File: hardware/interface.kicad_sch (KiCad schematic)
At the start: 26 parts, among them P1 TS2068_Edge, SW1 TS Reset, SW2 NMI, U1 74LVC245APW, U12 74LVC574APW, U13 74LVC574APW, U2 74LVC245APW, U3 74LVC245APW, U4 74LVC245APW, U6 74LVC32APW, U7 74LVC06AD, U8 74LVC245APW, U9 74LVC1G86

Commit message: Drop the DMA option: board fully routed, zero DRC errors
DMA_OPTION = False removes U8, U9, U12, U13 and six GPIOs; the data transceiver
takes DIR from /RD with its A side on the Z80 bus. Rerouted with the scripted
flow; finish order is DVDD before +3V3, supply pin 29 escapes through the freed
pad lanes, DVDD widened to 0.25 mm. No signal on either plane layer, all vias
0.6/0.3. Fab outputs regenerated; parts + fees $14.48 per board at 10 boards.

Co-Authored-By: Claude Fable 5.1 <noreply@anthropic.com>
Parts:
- removed C7, C8, C9: 100n, Capacitor_SMD:C_0603_1608Metric, symbol Device:C
- removed R4: 10k, Resistor_SMD:R_0603_1608Metric, symbol Device:R
- removed U12, U13: 74LVC574APW, Package_SO:TSSOP-20_4.4x6.5mm_P0.65mm, symbol 74xx:74LS574
- removed U8: 74LVC245APW, Package_SO:TSSOP-20_4.4x6.5mm_P0.65mm, symbol 74xx:74LS245
- removed U9: 74LVC1G86, Package_TO_SOT_SMD:SOT-23-5, symbol 74xGxx:74LVC1G86
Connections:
- net DATA_DIR is gone; now on net nRD: U3.1 (A->B)
- net D0: now also U3.3 (A1); no longer U3.12 (B6)
- net D1: now also U3.4 (A2); no longer U3.13 (B5)
- net D2: now also U3.5 (A3); no longer U3.14 (B4)
- net D3: now also U3.8 (A6); no longer U3.17 (B1)
- net D4: now also U3.9 (A7); no longer U3.18 (B0)
- net D5: now also U3.7 (A5); no longer U3.16 (B2)
- net D6: now also U3.6 (A4); no longer U3.15 (B3)
- net D7: now also U3.2 (A0); no longer U3.11 (B7)
- net MD0: now also U3.17 (B1); no longer U3.8 (A6)
- net MD1: now also U3.16 (B2); no longer U3.7 (A5)
- net MD2: now also U3.15 (B3); no longer U3.6 (A4)
- net MD3: now also U3.12 (B6); no longer U3.3 (A1)
- net MD4: now also U3.11 (B7); no longer U3.2 (A0)
- net MD5: now also U3.13 (B5); no longer U3.4 (A2)
- net MD6: now also U3.14 (B4); no longer U3.5 (A3)
- net MD7: now also U3.18 (B0); no longer U3.9 (A7)
- no-connect marks 21 -> 16

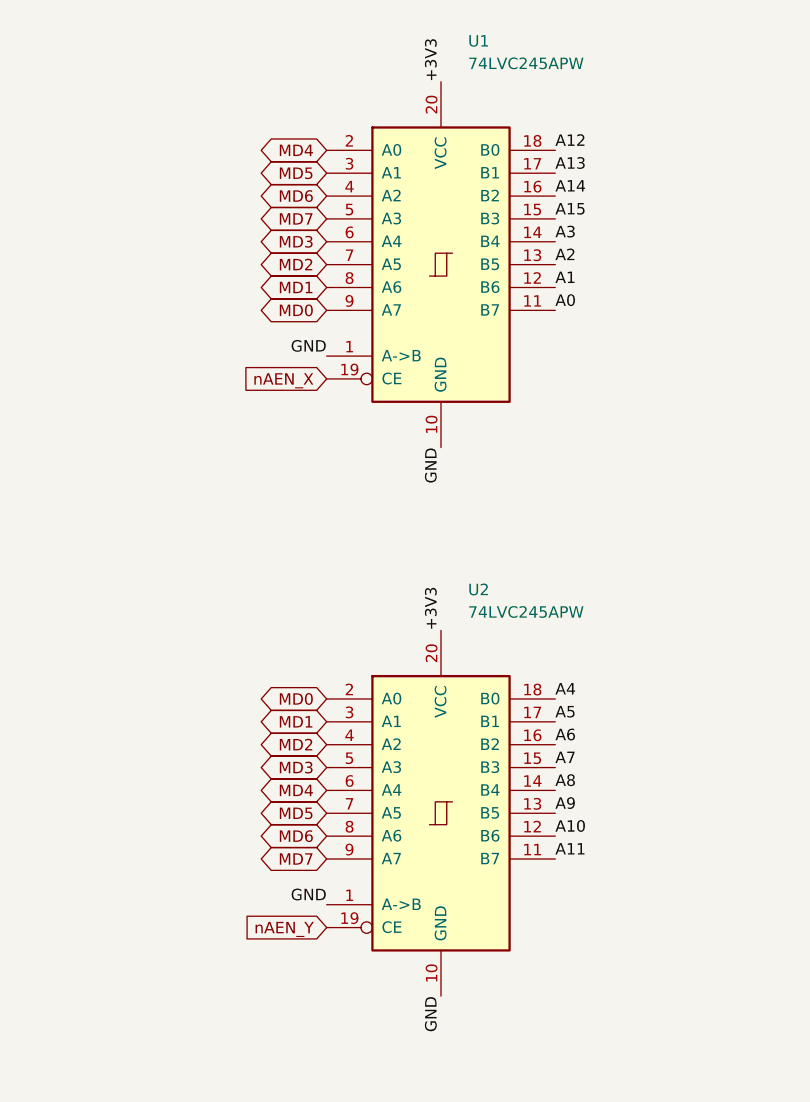
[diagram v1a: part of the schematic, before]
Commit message: Plain address bytes in hardware; DVDD spine and bottom-row fan pre-routed
U1 delivers A0-A7 and U2 A8-A15 on MD0-MD7 (U2 over its fingers, U1 in the row
above fed from both sides), so the firmware sees ordinary addresses. preroute.py
now also fixes the DVDD spine under the package, the inner 3.3 V supply links,
pin 51's capacitor and a deterministic fan for the fully used bottom pad row.
OLED_DC moves to GP34. Exposed pad gets five ground vias. finish.py: DVDD first,
clearance-aware widening, hairline fixes, unused-via cleanup, overlapping pads.
Fully routed, zero DRC errors; fab outputs regenerated.

Co-Authored-By: Claude Fable 5.1 <noreply@anthropic.com>
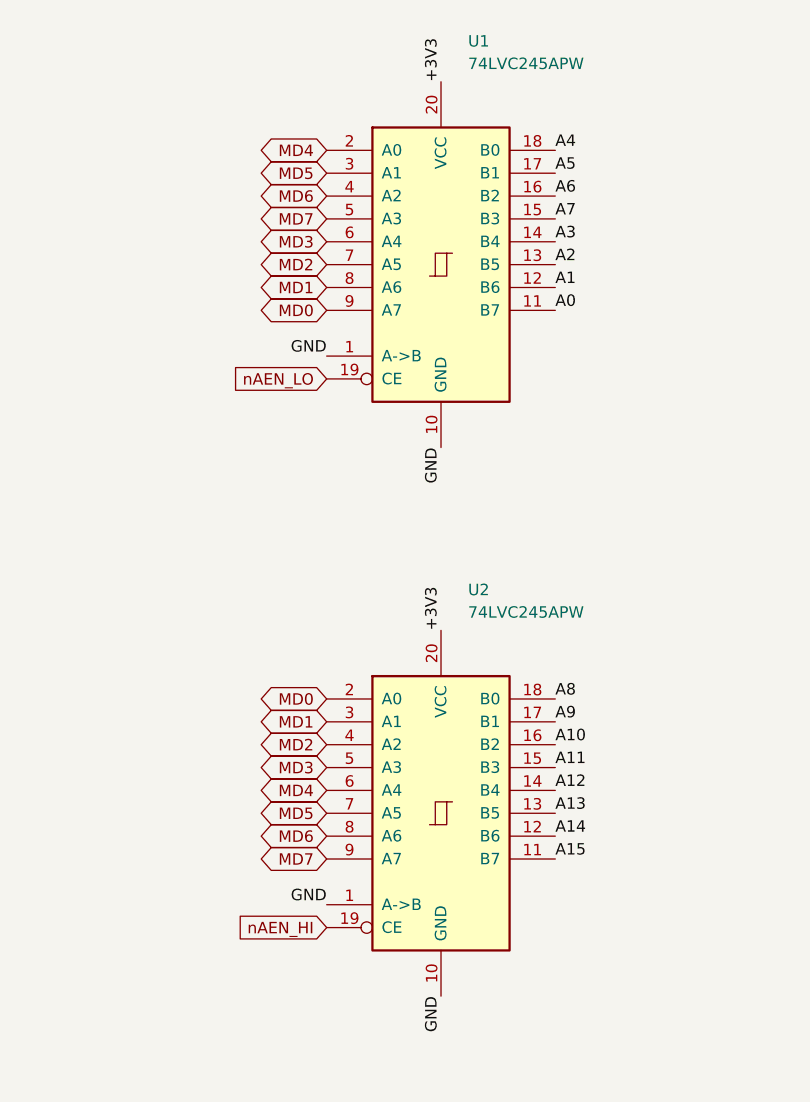
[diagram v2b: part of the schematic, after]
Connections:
- net A10: now also U2.16 (B2); no longer U2.12 (B6)
- net A11: now also U2.15 (B3); no longer U2.11 (B7)
- net A12: now also U2.14 (B4); no longer U1.18 (B0)
- net A13: now also U2.13 (B5); no longer U1.17 (B1)
- net A14: now also U2.12 (B6); no longer U1.16 (B2)
- net A15: now also U2.11 (B7); no longer U1.15 (B3)
- net A4: now also U1.18 (B0); no longer U2.18 (B0)
- net A5: now also U1.17 (B1); no longer U2.17 (B1)
- net A6: now also U1.16 (B2); no longer U2.16 (B2)
- net A7: now also U1.15 (B3); no longer U2.15 (B3)
- net A8: now also U2.18 (B0); no longer U2.14 (B4)
- net A9: now also U2.17 (B1); no longer U2.13 (B5)
- net nAEN_X renamed nAEN_LO
- net nAEN_Y renamed nAEN_HI
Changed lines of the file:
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@@
   (label "A3" (at 162.56 46.99 0) (effects (font (size 1.27 1.27)) (justify left bottom)))
   (global_label "MD3" (shape bidirectional) (at 137.16 46.99 180) (effects (font (size 1.27 1.27)) (justify right)))
-  (label "A15" (at 162.56 44.45 0) (effects (font (size 1.27 1.27)) (justify left bottom)))
+  (label "A7" (at 162.56 44.45 0) (effects (font (size 1.27 1.27)) (justify left bottom)))
   (global_label "MD7" (shape bidirectional) (at 137.16 44.45 180) (effects (font (size 1.27 1.27)) (justify right)))
-  (label "A14" (at 162.56 41.91 0) (effects (font (size 1.27 1.27)) (justify left bottom)))
+  (label "A6" (at 162.56 41.91 0) (effects (font (size 1.27 1.27)) (justify left bottom)))
   (global_label "MD6" (shape bidirectional) (at 137.16 41.91 180) (effects (font (size 1.27 1.27)) (justify right)))
-  (label "A13" (at 162.56 39.37 0) (effects (font (size 1.27 1.27)) (justify left bottom)))
+  (label "A5" (at 162.56 39.37 0) (effects (font (size 1.27 1.27)) (justify left bottom)))
   (global_label "MD5" (shape bidirectional) (at 137.16 39.37 180) (effects (font (size 1.27 1.27)) (justify right)))
-  (label "A12" (at 162.56 36.83 0) (effects (font (size 1.27 1.27)) (justify left bottom)))
+  (label "A4" (at 162.56 36.83 0) (effects (font (size 1.27 1.27)) (justify left bottom)))
   (global_label "MD4" (shape bidirectional) (at 137.16 36.83 180) (effects (font (size 1.27 1.27)) (justify right)))
   (label "GND" (at 137.16 59.69 180) (effects (font (size 1.27 1.27)) (justify right bottom)))
-  (global_label "nAEN_X" (shape input) (at 137.16 62.23 180) (effects (font (size 1.27 1.27)) (justify right)))
+  (global_label "nAEN_LO" (shape input) (at 137.16 62.23 180) (effects (font (size 1.27 1.27)) (justify right)))
   (label "+3V3" (at 149.86 29.21 90) (effects (font (size 1.27 1.27)) (justify left bottom)))
   (label "GND" (at 149.86 69.85 270) (effects (font (size 1.27 1.27)) (justify right bottom)))
@@
     (instances (project "tspico-v3" (path "/9088d141-8624-4d5c-91a9-7a3a7a90b3cc/a611a6fb-5e55-4c31-9c90-ae90d05d13a4" (reference "U2") (unit 1))))
   )
-  (label "A11" (at 162.56 115.57 0) (effects (font (size 1.27 1.27)) (justify left bottom)))
+  (label "A15" (at 162.56 115.57 0) (effects (font (size 1.27 1.27)) (justify left bottom)))
   (global_label "MD7" (shape bidirectional) (at 137.16 115.57 180) (effects (font (size 1.27 1.27)) (justify right)))
-  (label "A10" (at 162.56 113.03 0) (effects (font (size 1.27 1.27)) (justify left bottom)))
+  (label "A14" (at 162.56 113.03 0) (effects (font (size 1.27 1.27)) (justify left bottom)))
   (global_label "MD6" (shape bidirectional) (at 137.16 113.03 180) (effects (font (size 1.27 1.27)) (justify right)))
-  (label "A9" (at 162.56 110.49 0) (effects (font (size 1.27 1.27)) (justify left bottom)))
+  (label "A13" (at 162.56 110.49 0) (effects (font (size 1.27 1.27)) (justify left bottom)))
   (global_label "MD5" (shape bidirectional) (at 137.16 110.49 180) (effects (font (size 1.27 1.27)) (justify right)))
-  (label "A8" (at 162.56 107.95 0) (effects (font (size 1.27 1.27)) (justify left bottom)))
+  (label "A12" (at 162.56 107.95 0) (effects (font (size 1.27 1.27)) (justify left bottom)))
   (global_label "MD4" (shape bidirectional) (at 137.16 107.95 180) (effects (font (size 1.27 1.27)) (justify right)))
-  (label "A7" (at 162.56 105.41 0) (effects (font (size 1.27 1.27)) (justify left bottom)))
+  (label "A11" (at 162.56 105.41 0) (effects (font (size 1.27 1.27)) (justify left bottom)))
   (global_label "MD3" (shape bidirectional) (at 137.16 105.41 180) (effects (font (size 1.27 1.27)) (justify right)))
-  (label "A6" (at 162.56 102.87 0) (effects (font (size 1.27 1.27)) (justify left bottom)))
+  (label "A10" (at 162.56 102.87 0) (effects (font (size 1.27 1.27)) (justify left bottom)))
   (global_label "MD2" (shape bidirectional) (at 137.16 102.87 180) (effects (font (size 1.27 1.27)) (justify right)))
-  (label "A5" (at 162.56 100.33 0) (effects (font (size 1.27 1.27)) (justify left bottom)))
+  (label "A9" (at 162.56 100.33 0) (effects (font (size 1.27 1.27)) (justify left bottom)))
   (global_label "MD1" (shape bidirectional) (at 137.16 100.33 180) (effects (font (size 1.27 1.27)) (justify right)))
-  (label "A4" (at 162.56 97.79 0) (effects (font (size 1.27 1.27)) (justify left bottom)))
+  (label "A8" (at 162.56 97.79 0) (effects (font (size 1.27 1.27)) (justify left bottom)))
   (global_label "MD0" (shape bidirectional) (at 137.16 97.79 180) (effects (font (size 1.27 1.27)) (justify right)))
   (label "GND" (at 137.16 120.65 180) (effects (font (size 1.27 1.27)) (justify right bottom)))
-  (global_label "nAEN_Y" (shape input) (at 137.16 123.19 180) (effects (font (size 1.27 1.27)) (justify right)))
+  (global_label "nAEN_HI" (shape input) (at 137.16 123.19 180) (effects (font (size 1.27 1.27)) (justify right)))
   (label "+3V3" (at 149.86 90.17 90) (effects (font (size 1.27 1.27)) (justify left bottom)))
   (label "GND" (at 149.86 130.81 270) (effects (font (size 1.27 1.27)) (justify right bottom)))
